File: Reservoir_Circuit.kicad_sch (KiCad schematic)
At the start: 5 parts, among them J1 CN7, J2 CN10

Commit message: Added electrical components needed for this project
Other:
- company: (none) -> University of Waterloo, S2026 ECE 298 Group 12
- title: (none) -> ECE 298 Reservoir Circuit

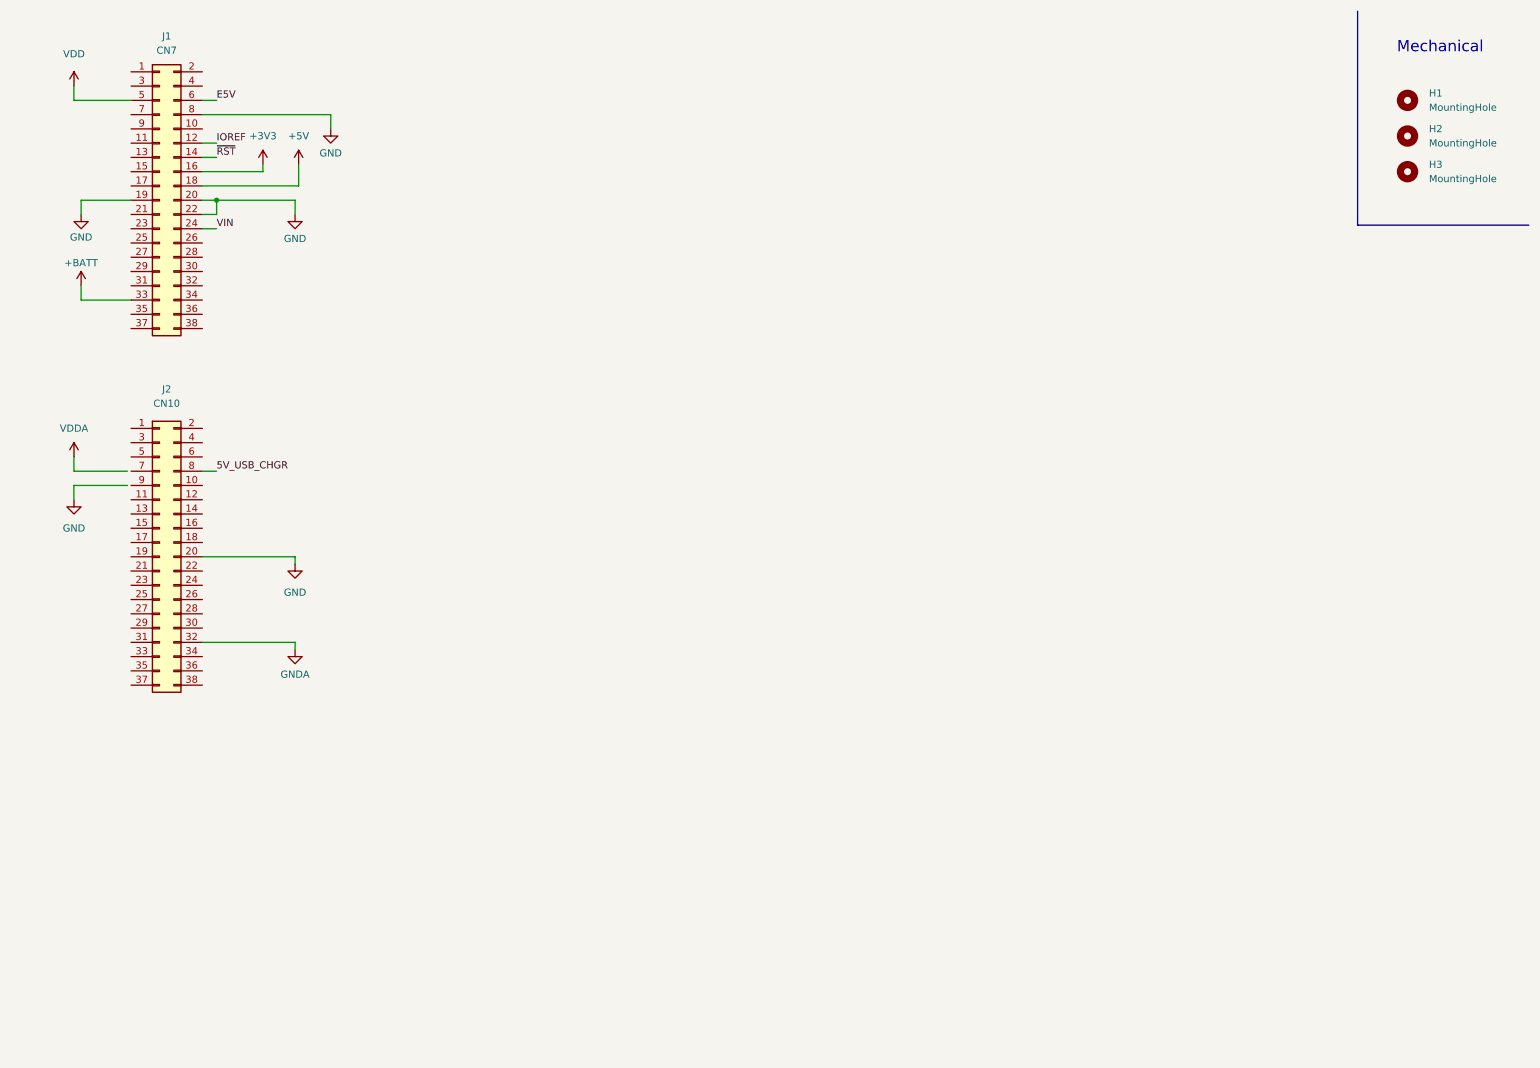
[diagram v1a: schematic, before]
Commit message: Set up net classes, and added bulk decoupling capacitors and an octal buffer
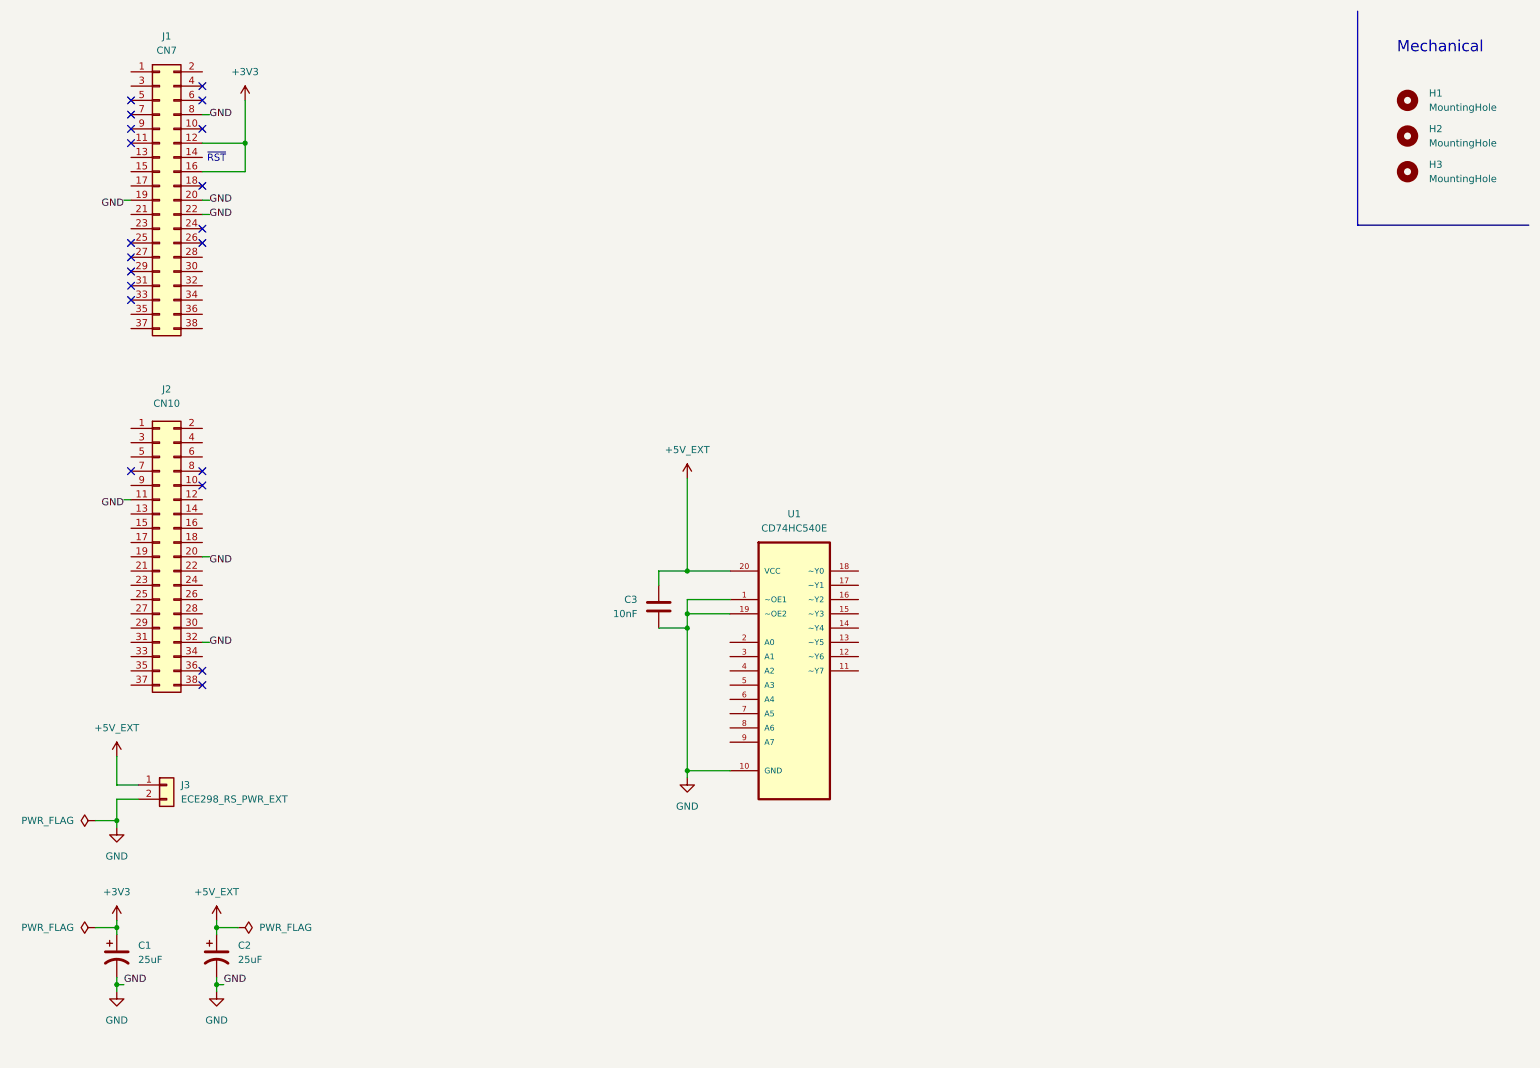
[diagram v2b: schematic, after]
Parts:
- added C1, C2: 25uF, Capacitor_SMD:C_Elec_3x5.4, symbol Device:C_Polarized_US
- added C3: 10nF, Capacitor_SMD:C_1206_3216Metric, symbol Device:C
- added J3: ECE298_RS_PWR_EXT, Connector_JST:JST_EH_B2B-EH-A_1x02_P2.50mm_Vertical, symbol Connector_Generic:Conn_01x02
- added U1: CD74HC540E, CD74HC540M:SOIC127P1030X265-20N, symbol CD74HC540E:CD74HC540E
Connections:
- net GNDA is gone; now on net GND: J2.32 (Pin_32)
- net IOREF is gone; now on net +3V3: J1.12 (Pin_12)
- net +3V3: now also C1.1
- net GND: now also J2.11 (Pin_11), C1.2, C2.2, C3.2, J3.2 (Pin_2), U1.1 (~OE1), U1.10 (GND), U1.19 (~OE2)
- net +5V: no longer names the net of J1.18 (Pin_18)
- net +BATT: no longer names the net of J1.33 (Pin_33)
- net 5V_USB_CHGR: no longer names the net of J2.8 (Pin_8)
- net E5V: no longer names the net of J1.6 (Pin_6)
- net VDD: no longer names the net of J1.5 (Pin_5)
- net VIN: no longer names the net of J1.24 (Pin_24)
- net ~{RST}: no longer names the net of J1.14 (Pin_14)
- new net +5V_EXT: C2.1, C3.1, J3.1 (Pin_1), U1.20 (VCC)
- no-connect marks 0 -> 20
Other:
- note added: "~{RST}"

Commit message: Finished wiring timer board
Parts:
- added C4: 10nF, Capacitor_SMD:C_1206_3216Metric, symbol Device:C
- added DS1: (no value), Connector_PinHeader_2.54mm:PinHeader_1x10_P2.54mm_Vertical, symbol ECE298:TIMER_BOARD
- added TP1: TP_GND, Connector_PinHeader_1.00mm:PinHeader_1x01_P1.00mm_Vertical, symbol Connector:TestPoint
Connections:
- net +5V_EXT: now also C4.1, DS1.10 (5V)
- net GND: now also C4.2, DS1.1 (GND), TP1.1
- net PC10: now reaches J1.1 (Pin_1)
- net PC10: now also U1.5 (A3)
- net PC11: now reaches J1.2 (Pin_2)
- net PC11: now also U1.4 (A2)
- net PC12: now reaches J1.3 (Pin_3)
- net PC12: now also U1.3 (A1)
- net PC9: now reaches J2.1 (Pin_1)
- net PC9: now also U1.2 (A0)
- net PB6: now reaches J2.17 (Pin_17)
- net PB6: now also U1.8 (A6)
- net PB5: now reaches J2.29 (Pin_29)
- net PB5: now also U1.9 (A7)
- net PB8: now reaches J2.3 (Pin_3)
- net PB8: now also U1.7 (A5)
- net PB9: now reaches J2.5 (Pin_5)
- net PB9: now also U1.6 (A4)
- net BCD_A0: now reaches U1.11 (~Y7)
- net BCD_A0: now also DS1.5 (A0)
- net BCD_A1: now reaches U1.12 (~Y6)
- net BCD_A1: now also DS1.4 (A1)
- net BCD_A2: now reaches U1.13 (~Y5)
- net BCD_A2: now also DS1.3 (A2)
- net BCD_A3: now reaches U1.14 (~Y4)
- net BCD_A3: now also DS1.2 (A3)
- net BCD_B0: now reaches U1.15 (~Y3)
- net BCD_B0: now also DS1.9 (B0)
- net BCD_B1: now reaches U1.16 (~Y2)
- net BCD_B1: now also DS1.8 (B1)
- net BCD_B2: now reaches U1.17 (~Y1)
- net BCD_B2: now also DS1.7 (B2)
- net BCD_B3: now reaches U1.18 (~Y0)
- net BCD_B3: now also DS1.6 (B3)

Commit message: Added hardware for ultrasonic sensor
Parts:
- added C5, C6: 10nF, Capacitor_SMD:C_1206_3216Metric, symbol Device:C
- added U2: HC-SR04, HC-SR04:XCVR_HC-SR04, symbol HC-SR04:HC-SR04
- added U3: (no value), CD74HC4049MT:SOIC127P600X175-16N, symbol CD74HC4049MT:CD74HC4049MT
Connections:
- net +3V3: now also C6.1, U3.1 (VCC)
- net +5V_EXT: now also C5.1, U2.1 (VCC)
- net GND: now also C5.2, C6.2, U2.4 (GND), U3.8 (GND)
- net PA1: now reaches J1.30 (Pin_30)
- net PA1: now also U3.15 (6Y)
- net PC8: now reaches J2.2 (Pin_2)
- net PC8: now also U2.2 (TRIG)
- new net ECHO: U2.3 (ECHO), U3.14 (6A)
- no-connect marks 20 -> 30
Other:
- moved on the sheet: C3, C4, DS1, U1

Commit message: Pulled unused input pins to GND
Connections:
- net GND: now also U3.11 (5A), U3.3 (1A), U3.5 (2A), U3.7 (3A), U3.9 (4A)
- no-connect marks 30 -> 25
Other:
- moved on the sheet: C6

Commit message: Added servo and RGB LED hardware
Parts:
- added C7: 10nF, Capacitor_SMD:C_1206_3216Metric, symbol Device:C
- added D1: LED_GRKB, LED_SMD:LED_Inolux_IN-PI554FCH_PLCC4_5.0x5.0mm_P3.2mm, symbol Device:LED_GRKB
- added M1: Motor_Servo, Connector_PinHeader_2.54mm:PinHeader_1x03_P2.54mm_Vertical, symbol Motor:Motor_Servo
- added R1, R2, R3: 100, PCM_SparkFun-Resistor:R_0603_1608Metric, symbol PCM_SparkFun-Resistor:R
- added U4: (no value), CD74HC4049MT:SOIC127P600X175-16N, symbol CD74HC4049MT:CD74HC4049MT
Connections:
- net +5V_EXT: now also C7.1, M1.2 (+), U4.1 (VCC)
- net GND: now also C7.2, D1.3 (K), M1.3 (-), U4.3 (1A), U4.7 (3A), U4.8 (GND)
- net PB7: now reaches J1.21 (Pin_21)
- net PB7: now also U4.5 (2A)
- net PA11: now reaches J2.14 (Pin_14)
- net PA11: now also U4.9 (4A)
- net PA8: now reaches J2.23 (Pin_23)
- net PA8: now also U4.14 (6A)
- net PA10: now reaches J2.33 (Pin_33)
- net PA10: now also U4.11 (5A)
- new net B: D1.4 (BA), R1.1
- new net B_BUF: R1.2, U4.15 (6Y)
- new net G: D1.1 (GA), R3.1
- new net G_BUF: R3.2, U4.10 (4Y)
- new net R: D1.2 (RA), R2.1
- new net R_BUF: R2.2, U4.12 (5Y)
- new net SERVO_SIG: M1.1 (PWM), U4.4 (2Y)
- no-connect marks 25 -> 27
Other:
- note added: "7-segment displays"
- note added: "Servo & RGB LED"
- note added: "Ultrasonic"
- moved on the sheet: C3, C5, C6, H1, H2, H3, U2, U3

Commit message: Added motor and motor driver
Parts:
- added C8: 10nF, Capacitor_SMD:C_1206_3216Metric, symbol Device:C
- added M2: Motor_DC, Connector_PinHeader_2.54mm:PinHeader_1x02_P2.54mm_Vertical, symbol Motor:Motor_DC
- added U5: L9110S, L9110S:SOIC127P599X172-8N, symbol L9110S:L9110S
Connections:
- net +5V_EXT: now also C8.1, U5.2 (VCC), U5.3 (VCC)
- net GND: now also C8.2, U5.5 (GND), U5.8 (GND)
- net PB0: now reaches J1.34 (Pin_34)
- net PB0: now also U5.6 (IA)
- net PB1: now reaches J2.24 (Pin_24)
- net PB1: now also U5.7 (IB)
- new net OA: M2.1 (+), U5.1 (OA)
- new net OB: M2.2 (-), U5.4 (OB)

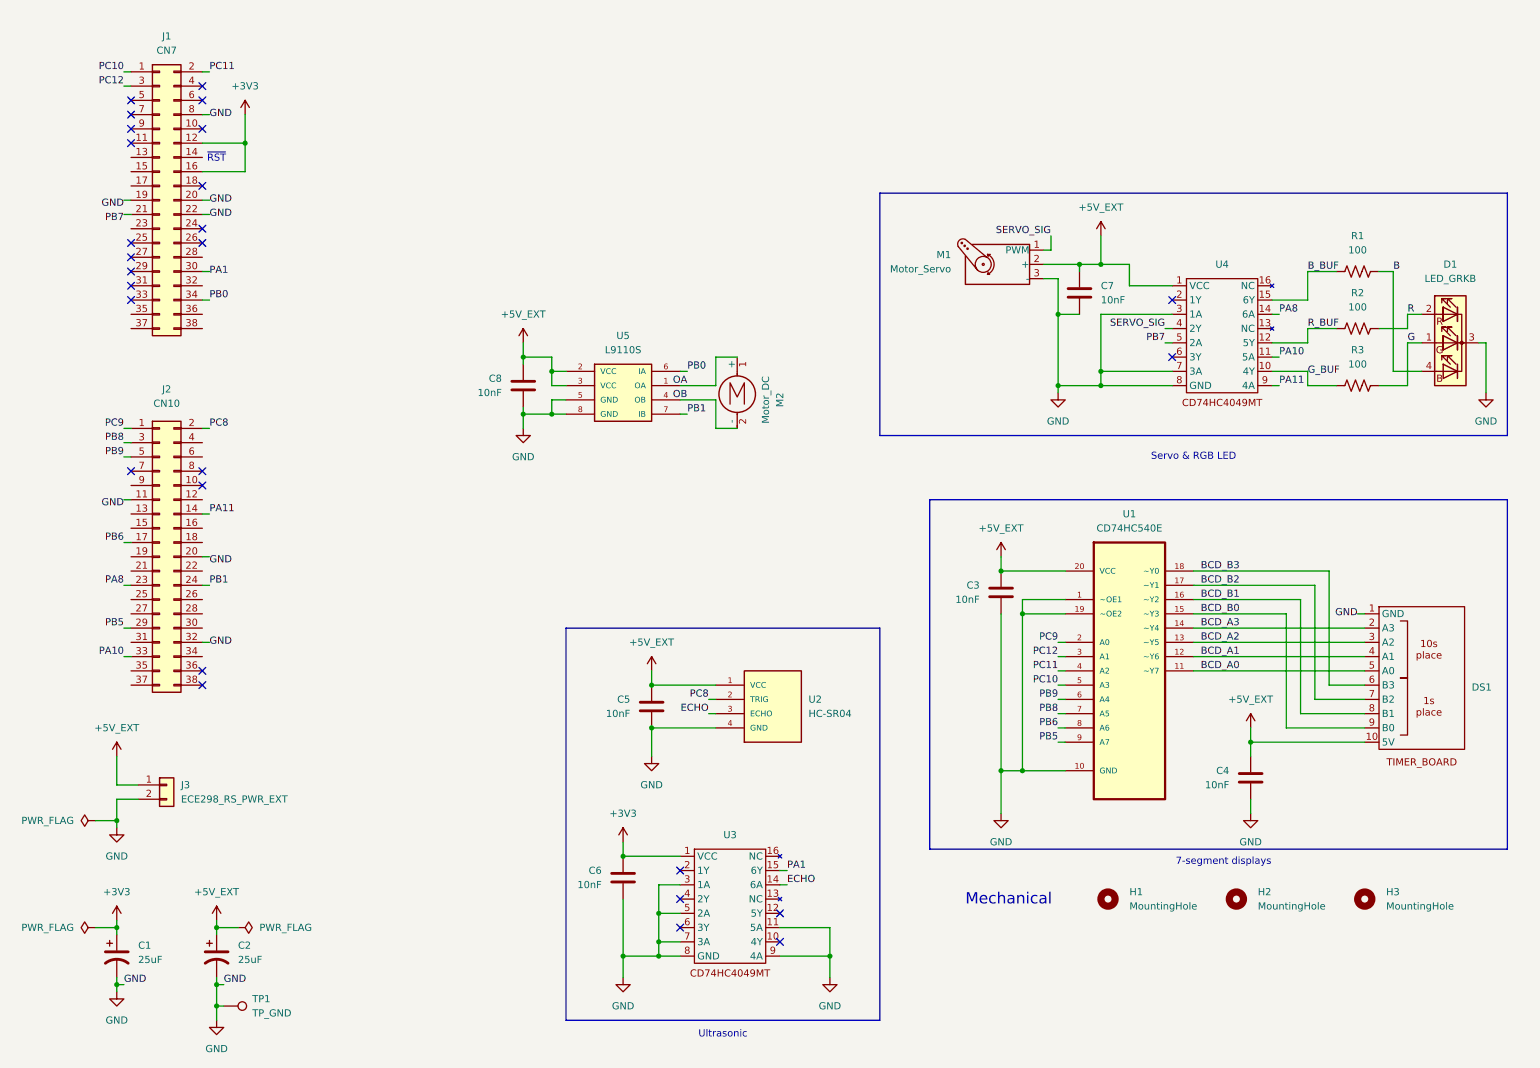
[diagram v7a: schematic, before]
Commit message: Added potentiometer and test points; clean ERC results
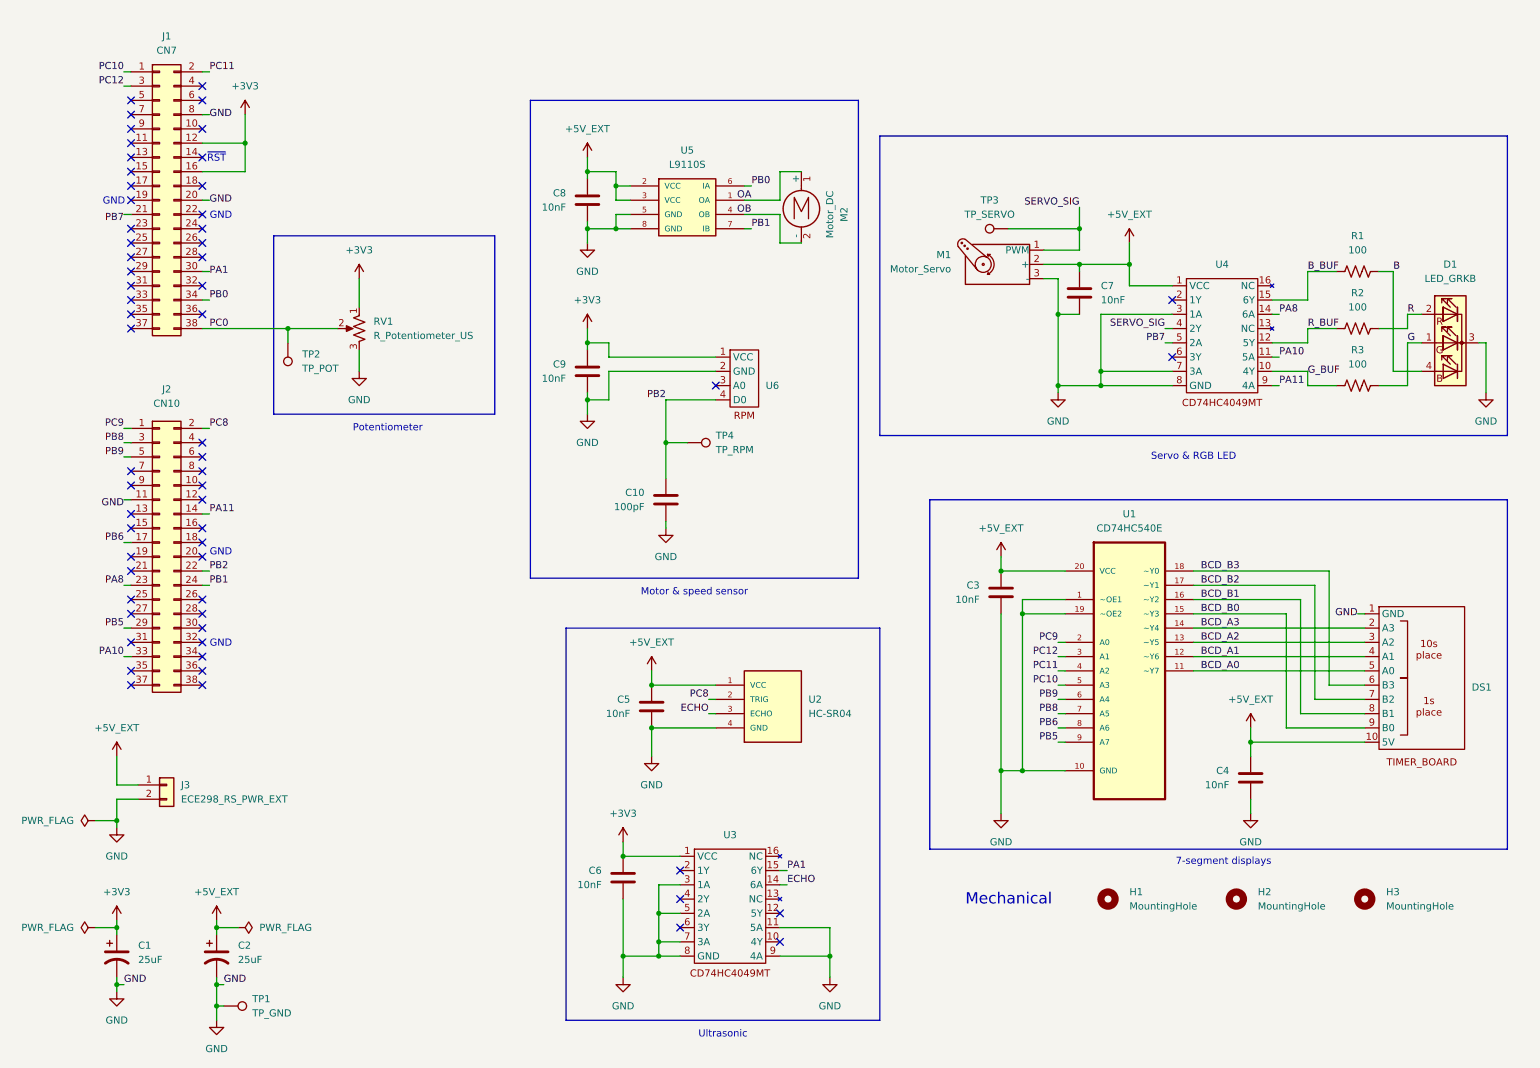
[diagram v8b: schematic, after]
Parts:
- added C10: 100pF, Capacitor_SMD:C_1206_3216Metric, symbol Device:C
- added C9: 10nF, Capacitor_SMD:C_1206_3216Metric, symbol Device:C
- added RV1: R_Potentiometer_US, Potentiometer_SMD:Potentiometer_Bourns_3314J_Vertical, symbol Device:R_Potentiometer_US
- added TP2: TP_POT, Connector_PinHeader_1.00mm:PinHeader_1x01_P1.00mm_Vertical, symbol Connector:TestPoint
- added TP3: TP_SERVO, Connector_PinHeader_1.00mm:PinHeader_1x01_P1.00mm_Vertical, symbol Connector:TestPoint
- added TP4: TP_RPM, Connector_PinHeader_1.00mm:PinHeader_1x01_P1.00mm_Vertical, symbol Connector:TestPoint
- added U6: (no value), Connector_PinHeader_2.54mm:PinHeader_1x04_P2.54mm_Vertical, symbol ECE298:SLOT_WHL_SPEED_SENSOR
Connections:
- net +3V3: now also C9.1, RV1.1, U6.1 (VCC)
- net GND: now also C10.2, C9.2, RV1.3, U6.2 (GND); no longer J1.19 (Pin_19), J1.22 (Pin_22), J2.20 (Pin_20), J2.32 (Pin_32)
- net SERVO_SIG: now also TP3.1
- net PC0: now reaches J1.38 (Pin_38)
- net PC0: now also RV1.2, TP2.1
- net PB2: now reaches J2.22 (Pin_22)
- net PB2: now also C10.1, TP4.1, U6.4 (D0)
- no-connect marks 27 -> 61
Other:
- note added: "GND"
- note added: "Motor & speed sensor"
- note added: "Potentiometer"
- moved on the sheet: C8, M2, U5
